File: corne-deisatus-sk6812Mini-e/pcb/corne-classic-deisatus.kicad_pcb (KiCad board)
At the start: 2 copper layers, 149.4 x 94.7 mm, 99 parts, among them J1 MJ-4PP-9, J2 OLED, J3 LED, P1 i2c-pin, P2 i2c-pin, SW1 SW_PUSH, SW10 SW_PUSH, SW11 SW_PUSH, SW12 SW_PUSH, SW13 SW_PUSH, SW14 SW_PUSH, SW15 SW_PUSH, SW16 SW_PUSH, SW17 SW_PUSH, SW18 SW_PUSH, SW19 SW_PUSH, SW2 SW_PUSH, SW20 SW_PUSH, SW21 SW_PUSH, SW22 SW_PUSH, SW3 SW_PUSH, SW4 SW_PUSH, SW5 SW_PUSH, SW6 SW_PUSH, SW7 SW_PUSH, SW8 SW_PUSH, SW9 SW_PUSH, U1 ProMicro

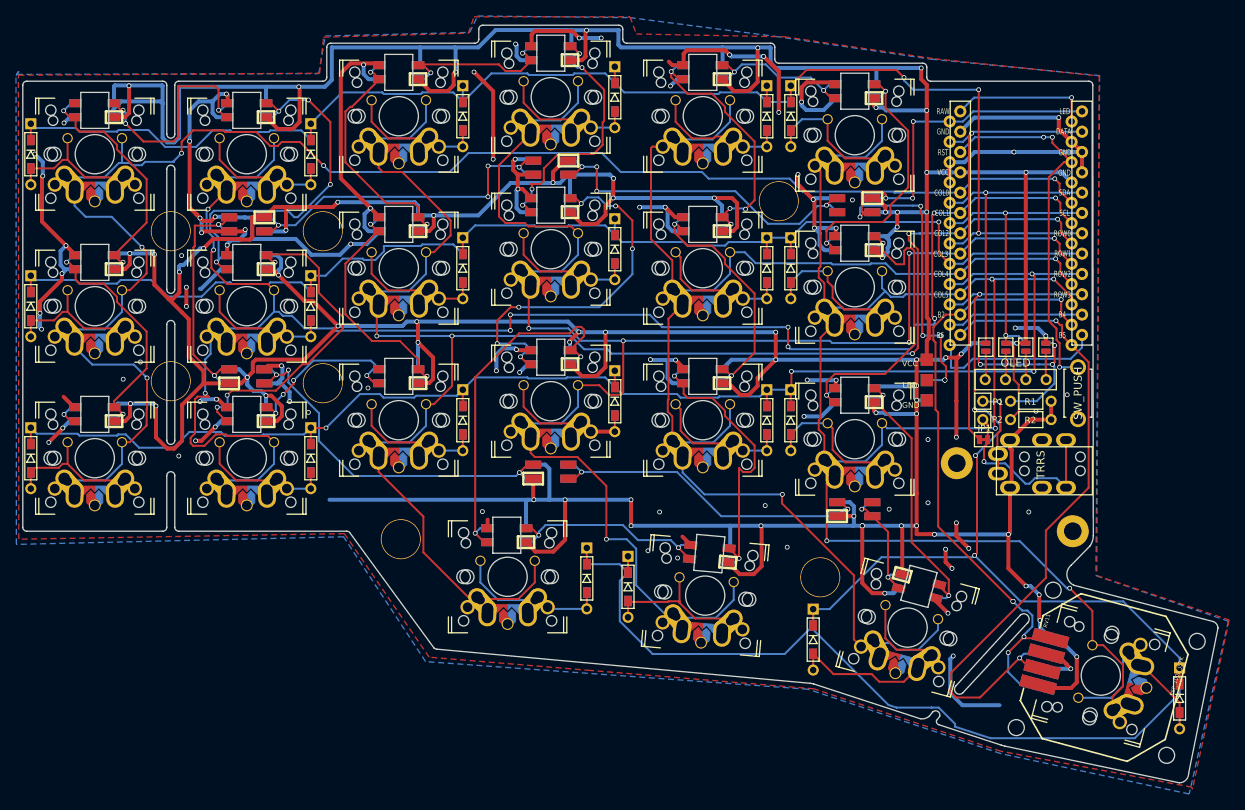
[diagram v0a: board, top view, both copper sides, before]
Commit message: added new pcb for new leds
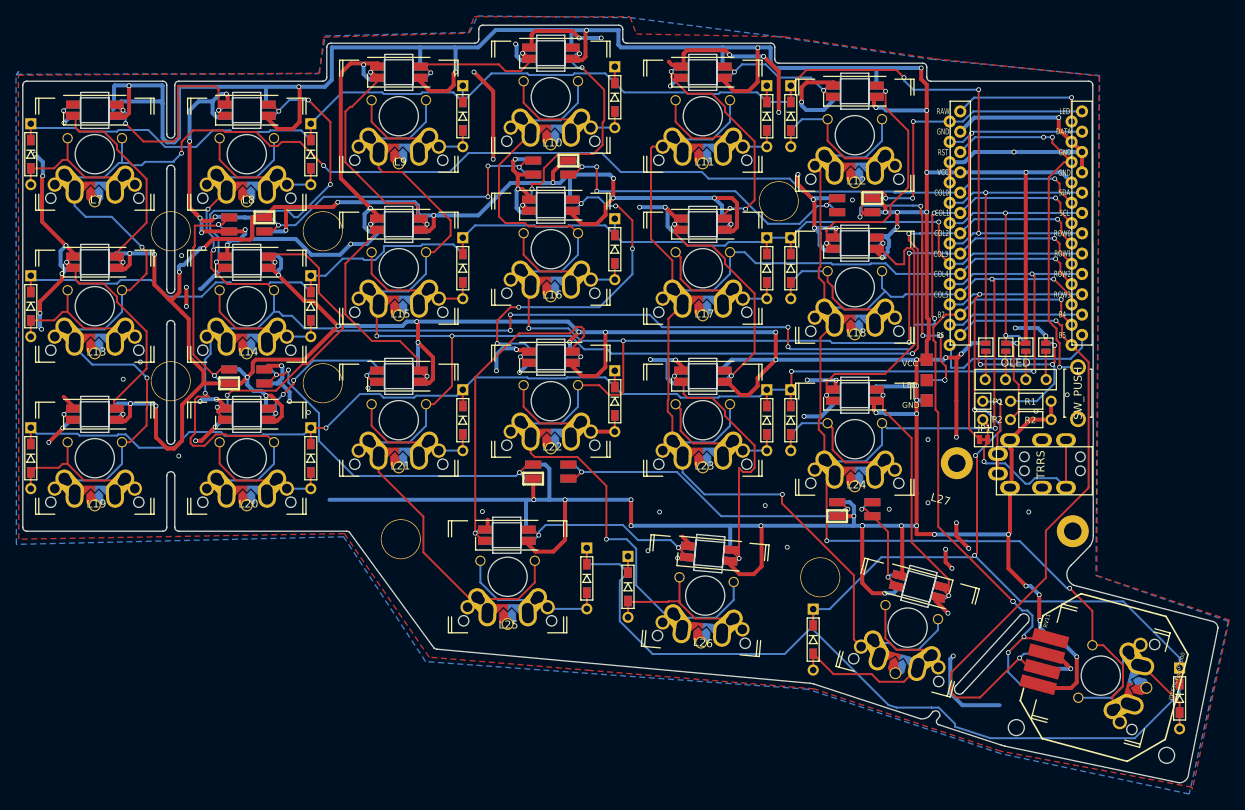
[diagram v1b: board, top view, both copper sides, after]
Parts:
- L10, L11, L12, L13, L14, L15, L16, L17, L18, L19, L20, L21, L22, L23, L24, L25, L26, L27, L7, L8, L9: value SK6812MINI -> SK6812MINI-E; footprint kbd:SK6812MINI_rev -> kbd:YS-SK6812MINI-E
- RV11: value PSP_1000_JSTK -> JOYSTICK-PSP1000; footprint HackPack_Footprints:JOYSTICK-PSP1000-reverse -> HackPack_Footprints:JOYSTICK-PSP1000
- SW20, SW21: footprint kailh-pg1425-x-switch:MX-ALPS-Choc-X-straight-crane2-u1.5 -> kailh-pg1425-x-switch:MX-ALPS-Choc-X-straight-crane2
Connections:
- L10 pad 1: Net-(L10-Pad1) -> VCC
- L10 pad 2: GND -> Net-(L10-Pad2)
- L10 pad 3: Net-(L10-Pad3) -> GND
- L10 pad 4: VCC -> Net-(L10-Pad4)
- L11 pad 1: Net-(L11-Pad1) -> VCC
- L11 pad 2: GND -> Net-(L11-Pad2)
- L11 pad 3: Net-(L11-Pad3) -> GND
- L11 pad 4: VCC -> Net-(L11-Pad4)
- L12 pad 1: Net-(L11-Pad3) -> VCC
- L12 pad 2: GND -> Net-(L11-Pad4)
- L12 pad 3: Net-(L12-Pad3) -> GND
- L12 pad 4: VCC -> Net-(L12-Pad4)
- L13 pad 1: Net-(L13-Pad1) -> VCC
- L13 pad 2: GND -> Net-(L13-Pad2)
- L13 pad 3: Net-(L13-Pad3) -> GND
- L13 pad 4: VCC -> Net-(L13-Pad4)
- L14 pad 1: Net-(L14-Pad1) -> VCC
- L14 pad 2: GND -> Net-(L14-Pad2)
- L14 pad 3: Net-(L14-Pad3) -> GND
- L14 pad 4: VCC -> Net-(L14-Pad4)
- L15 pad 1: Net-(L15-Pad1) -> VCC
- L15 pad 2: GND -> Net-(L15-Pad2)
- L15 pad 3: Net-(L15-Pad3) -> GND
- L15 pad 4: VCC -> Net-(L15-Pad4)
- L16 pad 1: Net-(L10-Pad3) -> VCC
- L16 pad 2: GND -> Net-(L10-Pad4)
- L16 pad 3: Net-(L16-Pad3) -> GND
- L16 pad 4: VCC -> Net-(L16-Pad4)
- L17 pad 1: Net-(L17-Pad1) -> VCC
- L17 pad 2: GND -> Net-(L17-Pad2)
- L17 pad 3: Net-(L11-Pad1) -> GND
- L17 pad 4: VCC -> Net-(L11-Pad2)
- L18 pad 1: Net-(L12-Pad3) -> VCC
- L18 pad 2: GND -> Net-(L12-Pad4)
- L18 pad 3: Net-(L18-Pad3) -> GND
- L18 pad 4: VCC -> Net-(L18-Pad4)
- L19 pad 1: Net-(L19-Pad1) -> VCC
- L19 pad 2: GND -> Net-(L19-Pad2)
- L19 pad 3: Net-(L13-Pad1) -> GND
- L19 pad 4: VCC -> Net-(L13-Pad2)
- L20 pad 1: Net-(L14-Pad3) -> VCC
- L20 pad 2: GND -> Net-(L14-Pad4)
- L20 pad 3: Net-(L20-Pad3) -> GND
- L20 pad 4: VCC -> Net-(L20-Pad4)
- L21 pad 1: Net-(L20-Pad3) -> VCC
- L21 pad 2: GND -> Net-(L20-Pad4)
- L21 pad 3: Net-(L15-Pad1) -> GND
- L21 pad 4: VCC -> Net-(L15-Pad2)
- L22 pad 1: Net-(L16-Pad3) -> VCC
- L22 pad 2: GND -> Net-(L16-Pad4)
- L22 pad 3: Net-(L22-Pad3) -> GND
- L22 pad 4: VCC -> Net-(L22-Pad4)
- L23 pad 1: Net-(L23-Pad1) -> VCC
- L23 pad 2: GND -> Net-(L23-Pad2)
- L23 pad 3: Net-(L17-Pad1) -> GND
- L23 pad 4: VCC -> Net-(L17-Pad2)
- L24 pad 1: Net-(L18-Pad3) -> VCC
- L24 pad 2: GND -> Net-(L18-Pad4)
- L24 pad 3: Net-(L24-Pad3) -> GND
- L24 pad 4: VCC -> Net-(L24-Pad4)
- L25 pad 1: Net-(L22-Pad3) -> VCC
- L25 pad 2: GND -> Net-(L22-Pad4)
- L25 pad 3: Net-(L25-Pad3) -> GND
- L25 pad 4: VCC -> Net-(L25-Pad4)
- L26 pad 1: Net-(L25-Pad3) -> VCC
- L26 pad 2: GND -> Net-(L25-Pad4)
- L26 pad 3: Net-(L23-Pad1) -> GND
- L26 pad 4: VCC -> Net-(L23-Pad2)
- L27 pad 1: Net-(L24-Pad3) -> VCC
- L27 pad 2: GND -> Net-(L24-Pad4)
- L27 pad 3: Net-(L27-Pad3) -> GND
- L27 pad 4: VCC -> Net-(L27-Pad4)
- L6 pad 1: Net-(L27-Pad3) -> Net-(L27-Pad4)
- L7 pad 1: Net-(L13-Pad3) -> VCC
- L7 pad 2: GND -> Net-(L13-Pad4)
- L7 pad 3: Net-(L7-Pad3) -> GND
- L7 pad 4: VCC -> Net-(L7-Pad4)
- L8 pad 1: Net-(L7-Pad3) -> VCC
- L8 pad 2: GND -> Net-(L7-Pad4)
- L8 pad 3: Net-(L14-Pad1) -> GND
- L8 pad 4: VCC -> Net-(L14-Pad2)
- L9 pad 1: Net-(L15-Pad3) -> VCC
- L9 pad 2: GND -> Net-(L15-Pad4)
- L9 pad 3: Net-(L10-Pad1) -> GND
- L9 pad 4: VCC -> Net-(L10-Pad2)
- RV11 pad 1: analogX -> AnalogX
- RV11 pad 3: analogY -> AnalogY
- U1 pad 11: Net-(U1-Pad11) -> AnalogY
- U1 pad 12: Net-(U1-Pad12) -> AnalogX
- U1 pad 13: analogY -> Net-(U1-Pad13)
- U1 pad 14: analogX -> Net-(U1-Pad14)
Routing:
- net GND: track 390.1 -> 250.1 mm, vias 86 -> 55
- net Net-(L13-Pad4): track 0.00 -> 28.5 mm, vias 0 -> 6
- net Net-(L11-Pad4): track 0.00 -> 23.8 mm, vias 0 -> 4
- net Net-(U1-Pad12): track 21.9 -> 0.00 mm
- net AnalogX: track 0.00 -> 21.9 mm
- net Net-(U1-Pad11): track 17.1 -> 0.00 mm
- net AnalogY: track 0.00 -> 17.1 mm
- net Net-(L10-Pad4): track 0.00 -> 14.4 mm, vias 0 -> 3
- net Net-(L12-Pad4): track 0.00 -> 12.0 mm, vias 0 -> 1
- net Net-(L11-Pad2): track 0.00 -> 10.8 mm, vias 0 -> 2
- net Net-(L24-Pad4): track 0.00 -> 9.35 mm, vias 0 -> 3
- net Net-(L17-Pad2): track 0.00 -> 9.30 mm, vias 0 -> 2
- net Net-(L20-Pad4): track 0.00 -> 9.00 mm, vias 0 -> 4
- net Net-(L22-Pad4): track 0.00 -> 8.77 mm, vias 0 -> 3
- net Net-(L13-Pad2): track 0.00 -> 6.52 mm, vias 0 -> 2
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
